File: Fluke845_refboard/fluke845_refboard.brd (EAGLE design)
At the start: 100 x 80 mm, 0 parts

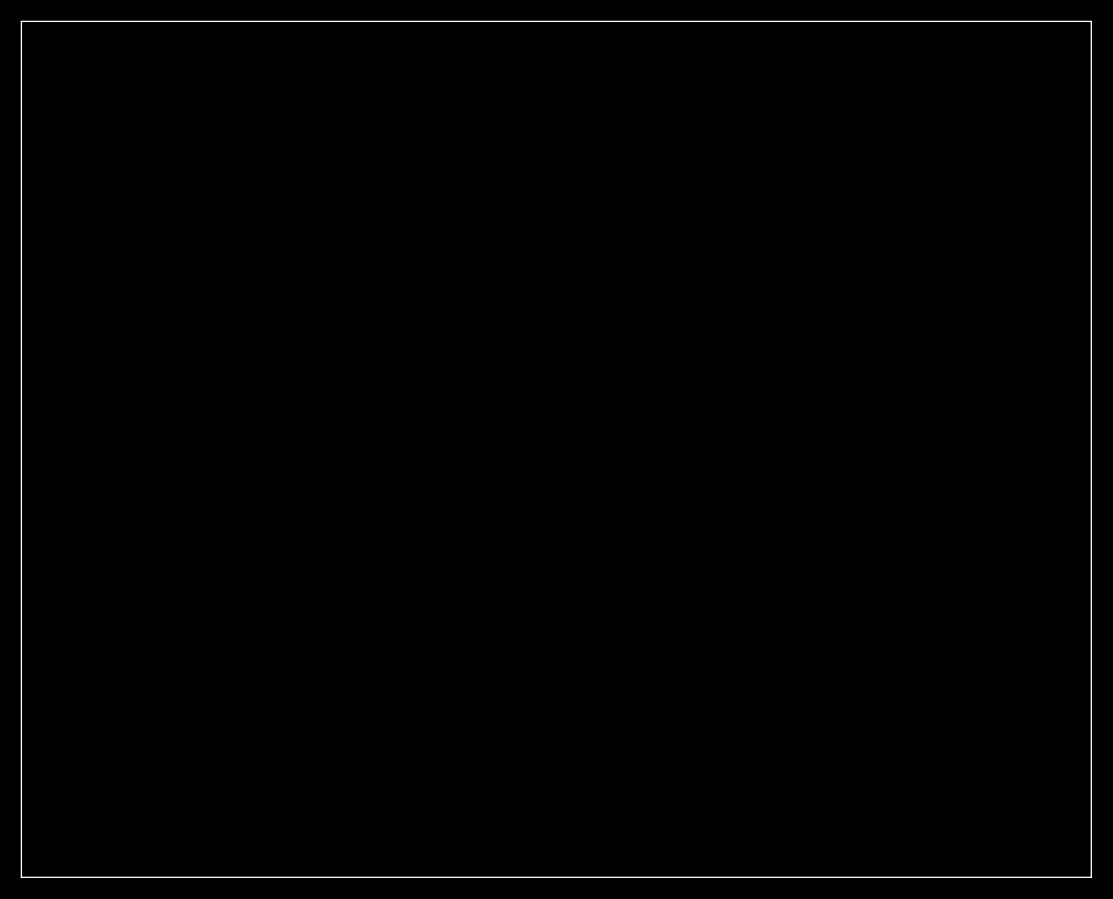
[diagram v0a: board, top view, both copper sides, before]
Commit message: * layed out fluke845 reference board
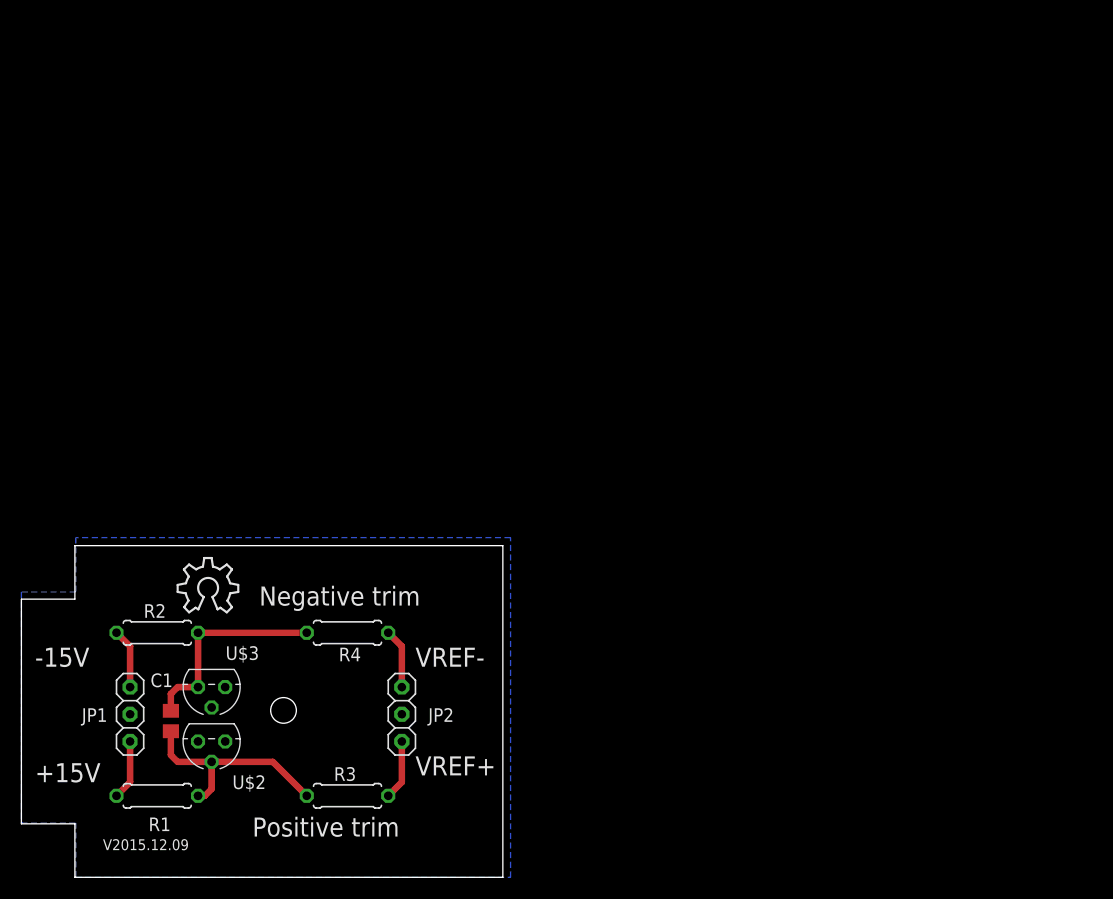
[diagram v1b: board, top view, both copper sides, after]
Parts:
- added C1: 10u, SquantorRCL:C0805
- added JP1, JP2: (no value), SquantorConnectors:1X03_SMALL
- added LOGO1: OSHW_LOGO_8MILX0200-NT, ohw-logo:OSHW_8X200_NOTEXT
- added R1, R2: 33k, SquantorRCL:0207/7
- added R3, R4: CALCULATE, SquantorRCL:0207/7
- added U$1: SUPERTRONIC37_51, SquantorPCBOutline:SUPERTRONIC_37_51MM
- added U$2, U$3: LT1004, SquantorLinearTechnology:TO92
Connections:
- new net +15V: JP1.1, R1.2
- new net -15V: JP1.3, R2.1
- new net GND: JP1.2, JP2.2, U$2.1, U$3.2
- new net N$1: C1.2, R2.2, R4.2, U$3.1
- new net N$2: C1.1, R1.1, R3.1, U$2.2
- new net VREF+: JP2.1, R3.2
- new net VREF-: JP2.3, R4.1
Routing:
- net N$2: track 0.00 -> 20.6 mm
- net N$1: track 0.00 -> 19.6 mm
- net VREF+: track 0.00 -> 5.61 mm
- net VREF-: track 0.00 -> 5.61 mm
- net +15V: track 0.00 -> 5.61 mm
- net -15V: track 0.00 -> 5.61 mm
- added copper zone on layer 16, net GND
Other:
- board size 100 x 80 mm -> 45 x 31 mm
- board text added: "+15V"
- board text added: "-15V"
- board text added: "Negative trim"
- board text added: "Positive trim"
- board text added: "V2015.12.09"
- board text added: "VREF+"
- board text added: "VREF-"
